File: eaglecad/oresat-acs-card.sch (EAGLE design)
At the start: 406 parts, among them J2 ORESAT-DEBUG-CONNECTOR-SOLAR, J6 J-SAMTEC-TFM-120-X1-XXX-D-RA, Q10 DMP2240UDM, Q11 MOSFET-PCH-SOT23-6, Q12 MOSFET-PCH-SOT23-6, Q13 PMV45EN, Q14 PMV45EN, Q15 DMP2240UDM, Q21 MOSFET-PCH-SOT23-6, Q22 MOSFET-PCH-SOT23-6, Q23 PMV45EN, Q24 PMV45EN, Q25 DMP2240UDM, Q26 MOSFET-PCH-SOT23-6, Q27 MOSFET-PCH-SOT23-6, Q28 PMV45EN, Q29 PMV45EN, Q30 DMP2240UDM, Q31 MOSFET-PCH-SOT23-6, Q32 MOSFET-PCH-SOT23-6, Q33 PMV45EN, Q34 PMV45EN, Q35 DMP2240UDM, Q6 MOSFET-PCH-SOT23-6, Q7 MOSFET-PCH-SOT23-6, Q8 PMV45EN, Q9 PMV45EN, U1 MAX892LEUA+T21-0036K-L, U10 MAX4211FETE, U11 MIC842LYC5, U12 MIC842LYC5, U13 BMI088, U14 TCAN330, U15 STM32F091C, U17 MAX7310ATE, U18 MAX4211FETE, U19 MIC842LYC5, U2 LTC4300A-1, U20 MIC842LYC5, U25 MAX7310ATE, U26 MAX4211FETE, U27 MIC842LYC5, U28 MIC842LYC5, U29 MAX7310ATE, U30 MAX4211FETE, U31 TPS62111RSA, U32 MIC842LYC5, U33 MIC842LYC5, U5 MAX7310ATE, U6 MAX4211FETE, U7 MIC842LYC5, U8 MIC842LYC5, U9 MAX7310ATE, X2 16MHZ-2.5x2mm

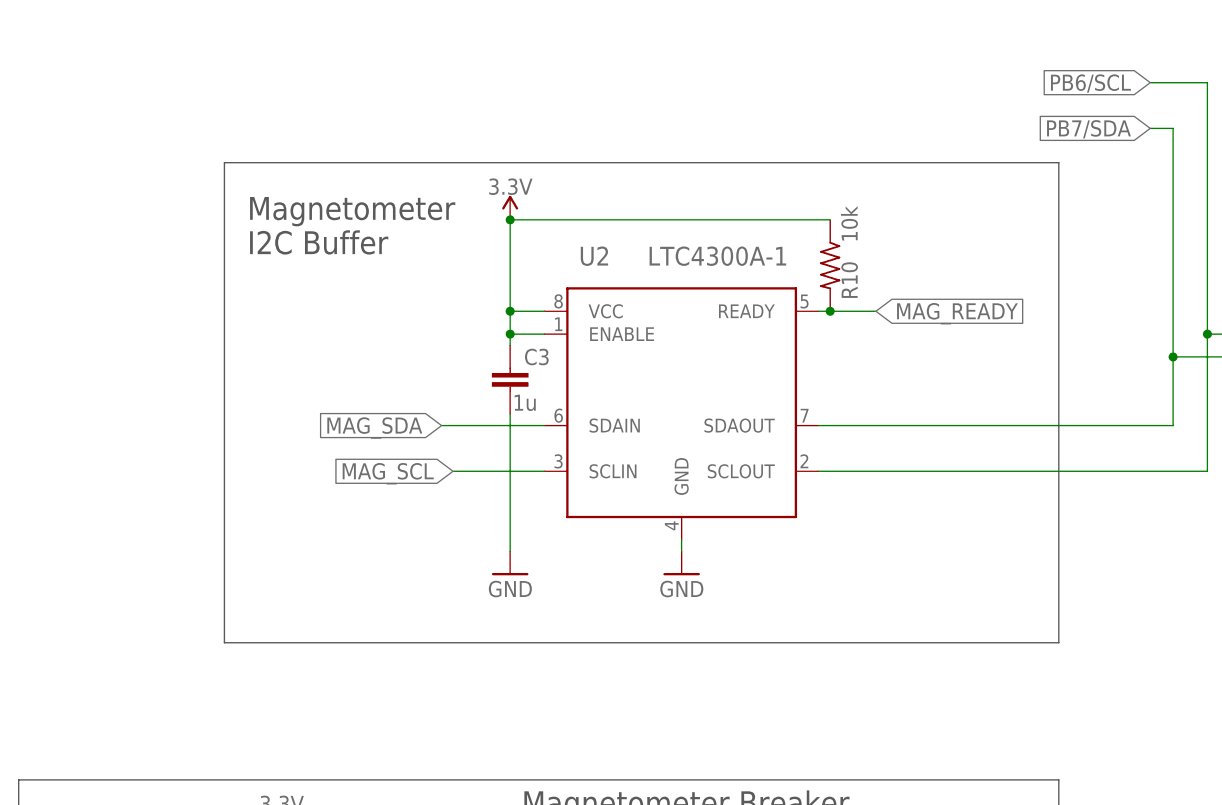
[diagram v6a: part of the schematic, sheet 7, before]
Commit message: Doubled up MAG_SDA and MAG_SCL on backplane connector to match backplane, and added pull up resistors for these signals. Updated BOM to reflect this.
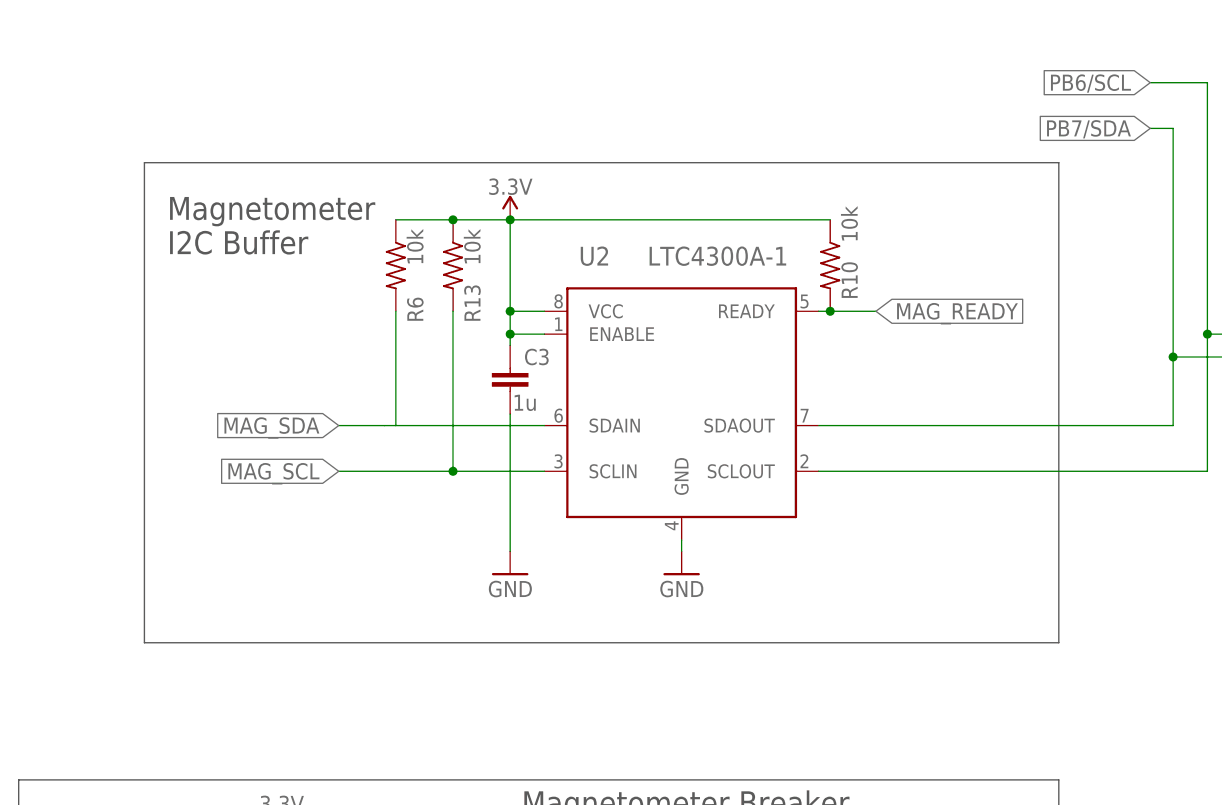
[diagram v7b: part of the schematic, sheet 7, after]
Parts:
- added R13, R6: 10k, oresat-rcl:R-US_0603-C-NOSILK
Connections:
- net 3.3V: now also R13.1, R6.1
- net MAG_SCL: now also J6.3, R13.2
- net MAG_SDA: now also J6.1, J6.2, R6.2; no longer J6.3
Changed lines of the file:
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@@
 <?xml version="1.0" encoding="utf-8"?>
 <!DOCTYPE eagle SYSTEM "eagle.dtd">
-<eagle version="9.6.1">
+<eagle version="9.5.1">
 <drawing>
 <settings>
@@
 <setting verticaltext="up"/>
 </settings>
-<grid distance="0.1" unitdist="inch" unit="inch" style="lines" multiple="1" display="no" altdistance="0.01" altunitdist="inch" altunit="inch"/>
+<grid distance="0.05" unitdist="inch" unit="inch" style="lines" multiple="1" display="no" altdistance="0.01" altunitdist="inch" altunit="inch"/>
 <layers>
 <layer number="1" name="Top" color="4" fill="1" visible="no" active="no"/>
@@
 <part name="GND13" library="supply1" library_urn="urn:adsk.eagle:library:371" deviceset="GND" device=""/>
 <part name="PCB1" library="oresat-cards" deviceset="ORESAT-CARD-V1.1" device="-NO-RF"/>
+<part name="R6" library="oresat-rcl" deviceset="R-US_" device="0603-C-NOSILK" value="10k">
+<spice>
+<pinmapping spiceprefix="R">
+<pinmap gate="G$1" pin="1" pinorder="1"/>
+<pinmap gate="G$1" pin="2" pinorder="2"/>
+</pinmapping>
+</spice>
+</part>
+<part name="R13" library="oresat-rcl" deviceset="R-US_" device="0603-C-NOSILK" value="10k">
+<spice>
+<pinmapping spiceprefix="R">
+<pinmap gate="G$1" pin="1" pinorder="1"/>
+<pinmap gate="G$1" pin="2" pinorder="2"/>
+</pinmapping>
+</spice>
+</part>
 </parts>
 <sheets>
@@
 <wire x1="107.95" y1="121.92" x2="107.95" y2="119.38" width="0.1524" layer="97"/>
 <wire x1="107.95" y1="119.38" x2="106.68" y2="119.38" width="0.1524" layer="97"/>
-<wire x1="106.68" y1="203.2" x2="107.95" y2="203.2" width="0.1524" layer="97"/>
-<wire x1="107.95" y1="203.2" x2="107.95" y2="200.66" width="0.1524" layer="97"/>
-<wire x1="107.95" y1="200.66" x2="106.68" y2="200.66" width="0.1524" layer="97"/>
 <wire x1="106.68" y1="187.96" x2="107.95" y2="187.96" width="0.1524" layer="97"/>
 <wire x1="107.95" y1="187.96" x2="107.95" y2="185.42" width="0.1524" layer="97"/>
@@
 <text x="109.22" y="180.34" size="1.778" layer="97">SPARE: Not used</text>
 <text x="109.22" y="185.42" size="1.778" layer="97">SPARE: Not used</text>
-<text x="109.22" y="200.66" size="1.778" layer="97">SPARE: Not used</text>
 </plain>
 <instances>
@@
 <segment>
 <pinref part="J6" gate="G$1" pin="4"/>
-<wire x1="101.6" y1="195.58" x2="127" y2="195.58" width="0.1524" layer="91"/>
-<wire x1="127" y1="195.58" x2="127" y2="198.12" width="0.1524" layer="91"/>
-<wire x1="127" y1="198.12" x2="128.27" y2="198.12" width="0.1524" layer="91"/>
+<wire x1="101.6" y1="195.58" x2="107.95" y2="195.58" width="0.1524" layer="91"/>
 <label x="128.27" y="198.12" size="2.54" layer="95" xref="yes"/>
+<pinref part="J6" gate="G$1" pin="3"/>
+<wire x1="128.27" y1="198.12" x2="107.95" y2="198.12" width="0.1524" layer="91"/>
+<wire x1="107.95" y1="198.12" x2="101.6" y2="198.12" width="0.1524" layer="91"/>
+<wire x1="107.95" y1="195.58" x2="107.95" y2="198.12" width="0.1524" layer="91"/>
+<junction x="107.95" y="198.12"/>
 </segment>
 </net>
 <net name="MAG_SDA" class="0">
 <segment>
-<pinref part="J6" gate="G$1" pin="3"/>
-<wire x1="101.6" y1="198.12" x2="125.73" y2="198.12" width="0.1524" layer="91"/>
-<wire x1="125.73" y1="198.12" x2="125.73" y2="203.2" width="0.1524" layer="91"/>
-<wire x1="125.73" y1="203.2" x2="128.27" y2="203.2" width="0.1524" layer="91"/>
 <label x="128.27" y="203.2" size="2.54" layer="95" xref="yes"/>
+<pinref part="J6" gate="G$1" pin="1"/>
+<wire x1="128.27" y1="203.2" x2="107.95" y2="203.2" width="0.1524" layer="91"/>
+<pinref part="J6" gate="G$1" pin="2"/>
+<wire x1="107.95" y1="203.2" x2="101.6" y2="203.2" width="0.1524" layer="91"/>
+<wire x1="101.6" y1="200.66" x2="107.95" y2="200.66" width="0.1524" layer="91"/>
+<wire x1="107.95" y1="200.66" x2="107.95" y2="203.2" width="0.1524" layer="91"/>
+<junction x="107.95" y="203.2"/>
 </segment>
 </net>
@@
 <plain>
 <wire x1="167.64" y1="143.51" x2="167.64" y2="196.85" width="0.1524" layer="97"/>
-<wire x1="167.64" y1="196.85" x2="74.93" y2="196.85" width="0.1524" layer="97"/>
-<wire x1="74.93" y1="196.85" x2="74.93" y2="143.51" width="0.1524" layer="97"/>
-<wire x1="74.93" y1="143.51" x2="167.64" y2="143.51" width="0.1524" layer="97"/>
-<text x="77.47" y="186.69" size="2.54" layer="97">Magnetometer
+<wire x1="167.64" y1="196.85" x2="66.04" y2="196.85" width="0.1524" layer="97"/>
+<wire x1="66.04" y1="196.85" x2="66.04" y2="143.51" width="0.1524" layer="97"/>
+<wire x1="66.04" y1="143.51" x2="167.64" y2="143.51" width="0.1524" layer="97"/>
+<text x="68.58" y="186.69" size="2.54" layer="97">Magnetometer
 I2C Buffer</text>
 <wire x1="52.07" y1="128.27" x2="167.64" y2="128.27" width="0.1524" layer="97"/>
@@
 <attribute name="VALUE" x="215.9" y="148.59" size="1.778" layer="96" rot="MR0"/>
 </instance>
+<instance part="R6" gate="R" x="93.98" y="185.42" smashed="yes" rot="R270">
+<attribute name="NAME" x="95.25" y="179.07" size="1.778" layer="95" rot="MR90"/>
+<attribute name="VALUE" x="95.25" y="185.42" size="1.778" layer="96" rot="MR90"/>
+</instance>
+<instance part="R13" gate="R" x="100.33" y="185.42" smashed="yes" rot="R270">
+<attribute name="NAME" x="101.6" y="179.07" size="1.778" layer="95" rot="MR90"/>
+<attribute name="VALUE" x="101.6" y="185.42" size="1.778" layer="96" rot="MR90"/>
+</instance>
 </instances>
 <busses>
@@
 <junction x="106.68" y="190.5"/>
 <pinref part="R10" gate="R" pin="1"/>
+<pinref part="R13" gate="R" pin="1"/>
+<wire x1="100.33" y1="190.5" x2="106.68" y2="190.5" width="0.1524" layer="91"/>
+<pinref part="R6" gate="R" pin="1"/>
+<wire x1="93.98" y1="190.5" x2="100.33" y2="190.5" width="0.1524" layer="91"/>
+<junction x="100.33" y="190.5"/>
 </segment>
 <segment>
@@
 <segment>
 <pinref part="U2" gate="G$1" pin="SDAIN"/>
-<wire x1="110.49" y1="167.64" x2="99.06" y2="167.64" width="0.1524" layer="91"/>
-<label x="99.06" y="167.64" size="1.778" layer="95" rot="R180" xref="yes"/>
+<wire x1="110.49" y1="167.64" x2="93.98" y2="167.64" width="0.1524" layer="91"/>
+<label x="87.63" y="167.64" size="1.778" layer="95" rot="R180" xref="yes"/>
+<pinref part="R6" gate="R" pin="2"/>
+<wire x1="92.71" y1="167.64" x2="87.63" y2="167.64" width="0.1524" layer="91"/>
+<wire x1="92.71" y1="167.64" x2="93.98" y2="167.64" width="0.1524" layer="91"/>
+<wire x1="93.98" y1="167.64" x2="93.98" y2="180.34" width="0.1524" layer="91"/>
 </segment>
 </net>
@@
 <pinref part="U2" gate="G$1" pin="SCLIN"/>
 <wire x1="110.49" y1="162.56" x2="100.33" y2="162.56" width="0.1524" layer="91"/>
-<label x="100.33" y="162.56" size="1.778" layer="95" rot="R180" xref="yes"/>
+<label x="87.63" y="162.56" size="1.778" layer="95" rot="R180" xref="yes"/>
+<pinref part="R13" gate="R" pin="2"/>
+<wire x1="100.33" y1="162.56" x2="87.63" y2="162.56" width="0.1524" layer="91"/>
+<wire x1="100.33" y1="162.56" x2="100.33" y2="180.34" width="0.1524" layer="91"/>
+<junction x="100.33" y="162.56"/>
 </segment>
 </net>

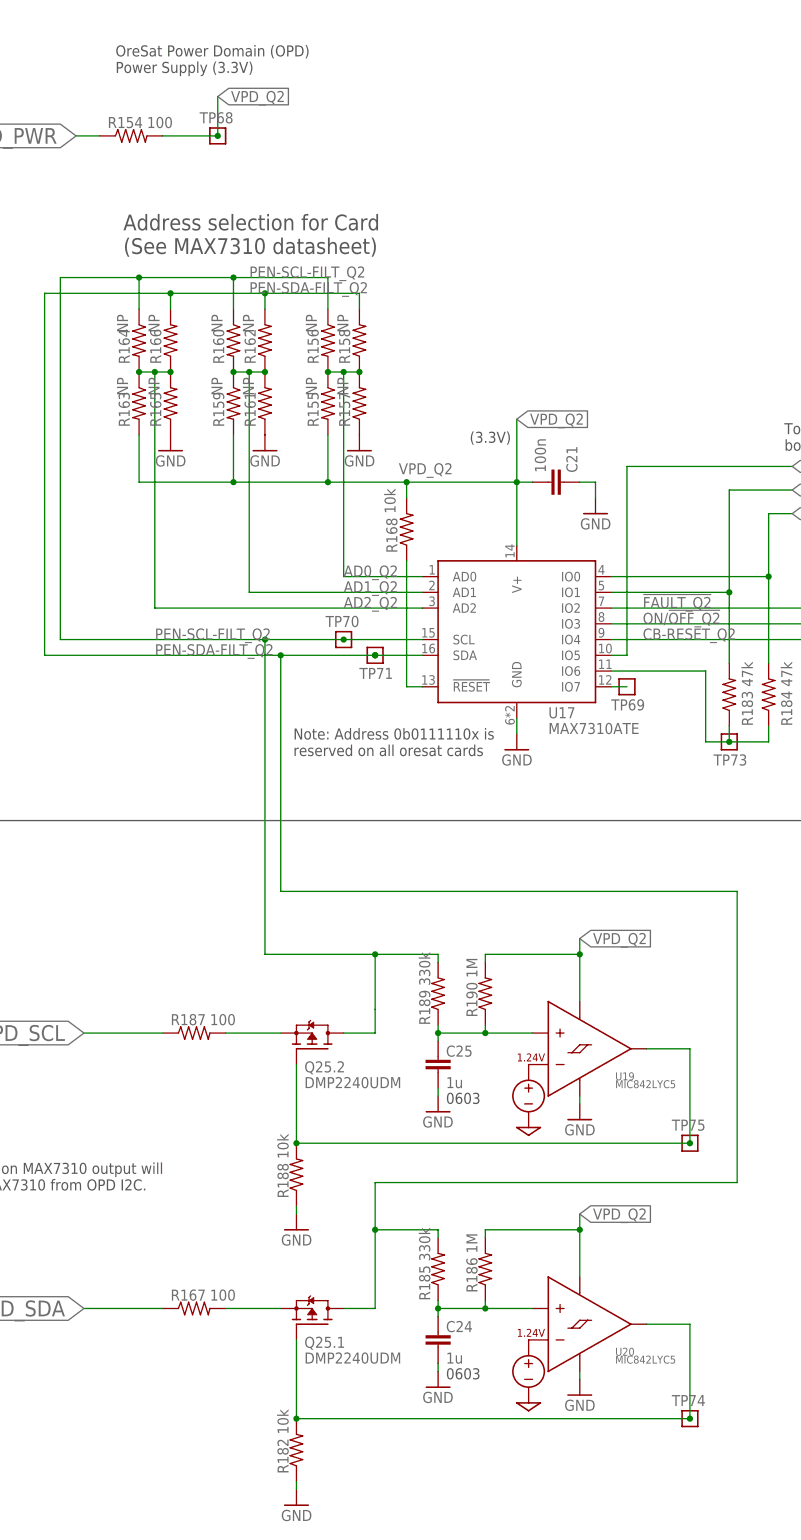
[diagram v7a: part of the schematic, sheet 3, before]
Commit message: Standardized passives to 0603 and changed all test points to circular footprint. Spaced out components in OPD for easier stuffing. Cleaned up names layer. Fixed OPD protection circuit to match OPD design block and changed R40 R78 R154 and R230 to 10 ohms to match design block.
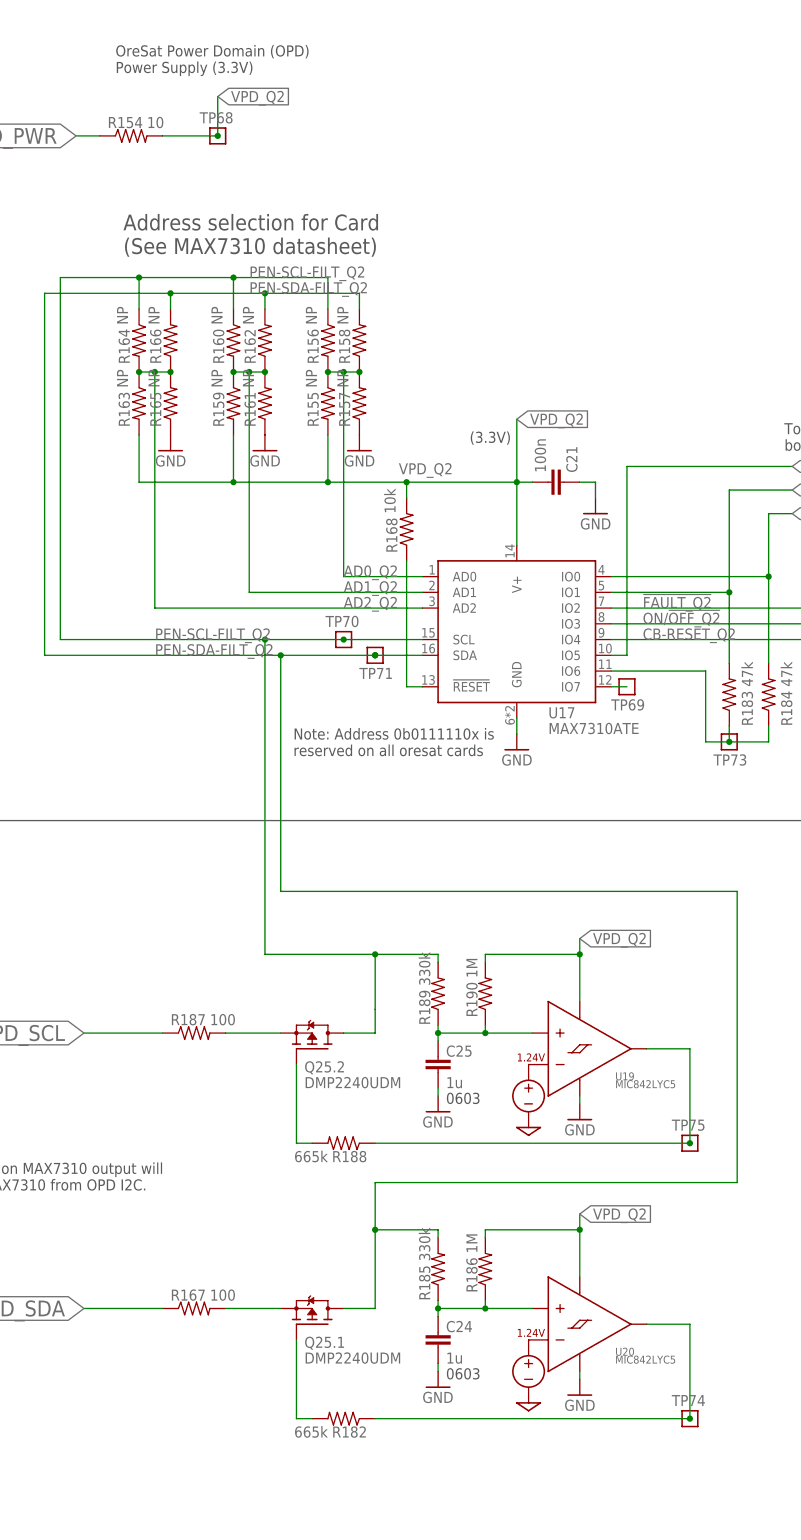
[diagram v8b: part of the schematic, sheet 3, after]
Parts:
- C10, C13, C14, C15, C23, C24, C25, C33, C34, C35, C8, C9: device oresat-rcl:C-EU0603-B-NOSILK -> oresat-rcl:C-EU0603-C-NOSILK
- C11, C12, C21, C22, C31, C32, C6, C7: device rcl_custom:C-EU0402-B-NOSILK -> oresat-rcl:C-EU0603-C-NOSILK
- R100, R101, R102, R103, R104, R105, R107, R108, R109, R110, R111, R113, R114, R153, R155, R156, R157, R158, R159, R160, R161, R162, R163, R164, R165, R166, R167, R168, R169, R170, R172, R173, R174, R175, R176, R177, R178, R179, R180, R181, R183, R184, R185, R186, R187, R189, R190, R229, R231, R232, R233, R234, R235, R236, R237, R238, R239, R240, R241, R242, R243, R244, R245, R246, R248, R249, R250, R251, R252, R253, R254, R255, R256, R257, R259, R260, R261, R262, R263, R265, R266, R39, R41, R42, R43, R44, R45, R46, R47, R48, R49, R50, R51, R52, R53, R54, R55, R56, R58, R59, R60, R61, R62, R63, R64, R65, R66, R67, R69, R70, R71, R72, R73, R75, R76, R77, R79, R80, R81, R82, R83, R84, R85, R86, R87, R88, R89, R90, R91, R92, R93, R94, R96, R97, R98, R99: device rcl_custom:R-US_0402-B-NOSILK -> oresat-rcl:R-US_0603-C-NOSILK
- R106, R112, R182, R188, R258, R264, R68, R74: value 10k -> 665k; device rcl_custom:R-US_0402-B-NOSILK -> oresat-rcl:R-US_0603-C-NOSILK
- R154, R230, R40, R78: value 100 -> 10; device rcl_custom:R-US_0402-B-NOSILK -> oresat-rcl:R-US_0603-C-NOSILK
- R268, R272: value 10k -> 665k
- TP10, TP100, TP101, TP102, TP103, TP104, TP105, TP11, TP12, TP13, TP14, TP15, TP16, TP17, TP19, TP2, TP21, TP23, TP24, TP25, TP26, TP27, TP28, TP29, TP30, TP31, TP32, TP33, TP34, TP35, TP36, TP37, TP38, TP39, TP4, TP40, TP41, TP42, TP43, TP44, TP45, TP61, TP62, TP63, TP64, TP65, TP66, TP67, TP68, TP69, TP70, TP71, TP72, TP73, TP74, TP75, TP9, TP91, TP92, TP93, TP94, TP95, TP96, TP97, TP98, TP99: value TEST-POINT -> TEST-POINT-LARGE-SQUARE; device Tova:TEST-POINT -> oresat-misc:TEST-POINT-LARGE-SQUARE
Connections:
- new net N$26: Q10.2.G, R74.2
- new net N$27: Q10.1.G, R68.2
- new net N$28: Q15.2.G, R112.2
- new net N$29: Q15.1.G, R106.2
- new net N$30: Q25.2.G, R188.2
- new net N$41: Q25.1.G, R182.2
- new net N$42: Q35.1.G, R258.2
- new net N$43: Q35.2.G, R264.2
- new net N$44: Q30.2.G, R272.2
- new net N$46: Q30.1.G, R268.2
- net GND: no longer R106.1, R112.1, R182.1, R188.1, R258.1, R264.1, R268.1, R272.1, R68.1, R74.1
- net N$17: now also R68.1; no longer Q10.1.G, R68.2
- net N$181: now also R106.1; no longer Q15.1.G, R106.2
- net N$184: now also R112.1; no longer Q15.2.G, R112.2
- net N$20: now also R74.1; no longer Q10.2.G, R74.2
- net N$217: now also R182.1; no longer Q25.1.G, R182.2
- net N$220: now also R188.1; no longer Q25.2.G, R188.2
- net N$253: now also R258.1; no longer Q35.1.G, R258.2
- net N$256: now also R264.1; no longer Q35.2.G, R264.2
- net N$71: now also R268.1; no longer Q30.1.G, R268.2
- net N$74: now also R272.1; no longer Q30.2.G, R272.2
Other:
- moved on the sheet: R106, R112, R182, R188, R258, R264, R268, R272, R68, R74
